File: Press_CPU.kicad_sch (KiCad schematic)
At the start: 100 parts, among them J2 2-215079-0, J3 Conn_01x16, J4 Conn_01x16, U1 APM32F405RGT6, U10 LMV321, U11 LMV321, U12 FM25W256, U13 LMV321, U14 LMV321, U15 LMV321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

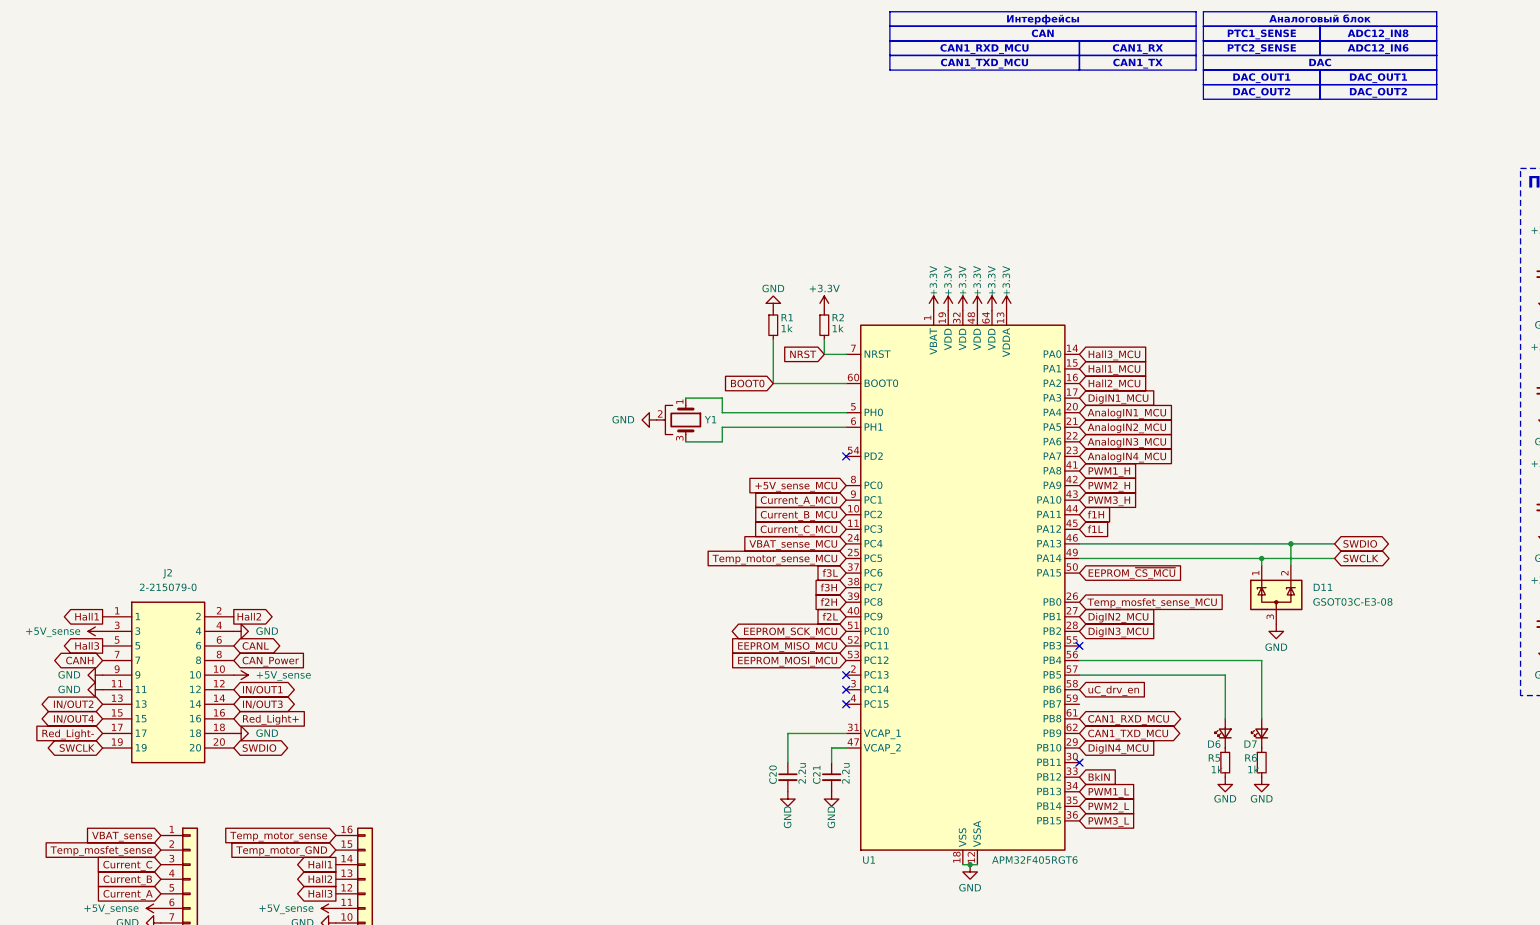
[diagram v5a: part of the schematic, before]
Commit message: VER1.0: первая готовая трассировка, требует обсуждения
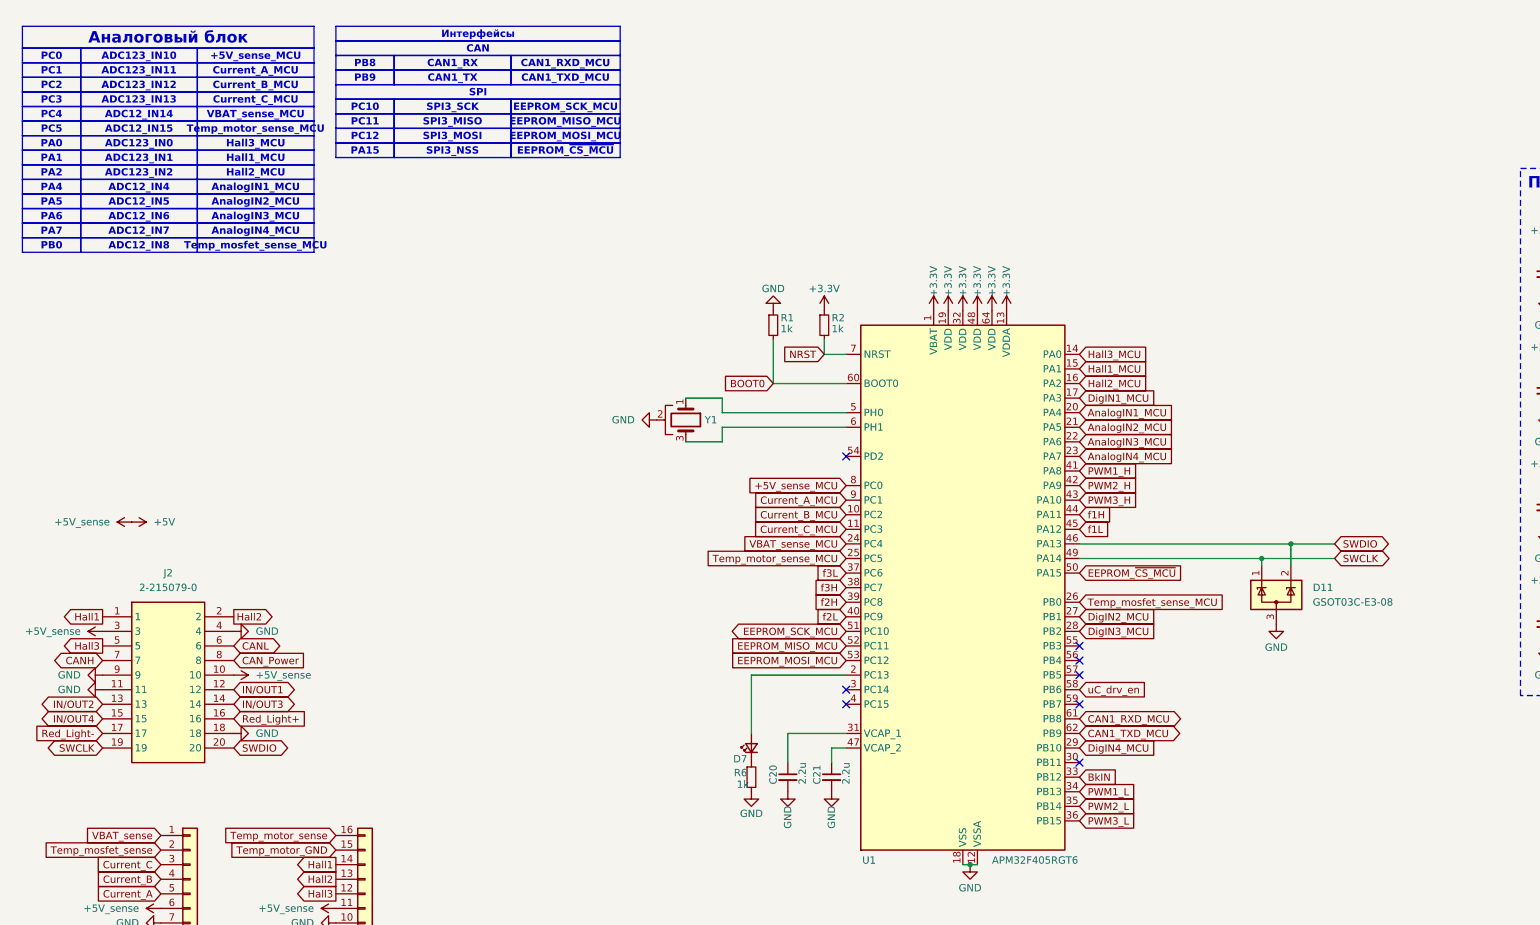
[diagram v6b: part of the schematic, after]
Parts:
- removed D6: ~, LED_SMD:LED_0603_1608Metric_Pad1.05x0.95mm_HandSolder, symbol Device:LED_Small
- removed R5: 1k, Resistor_SMD:R_0603_1608Metric_Pad0.98x0.95mm_HandSolder, symbol Device:R_Small
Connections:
- net +5V_sense is gone; now on net +5V: J2.10, J2.3, J3.6 (Pin_6), J4.11 (Pin_11), R65.1, R66.1
- net at U1.2 (PC13): now also D7.2 (A)
- net at U1.56 (PB4): no longer D7.2 (A)
- no-connect marks 11 -> 13
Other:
- moved on the sheet: D7, R6

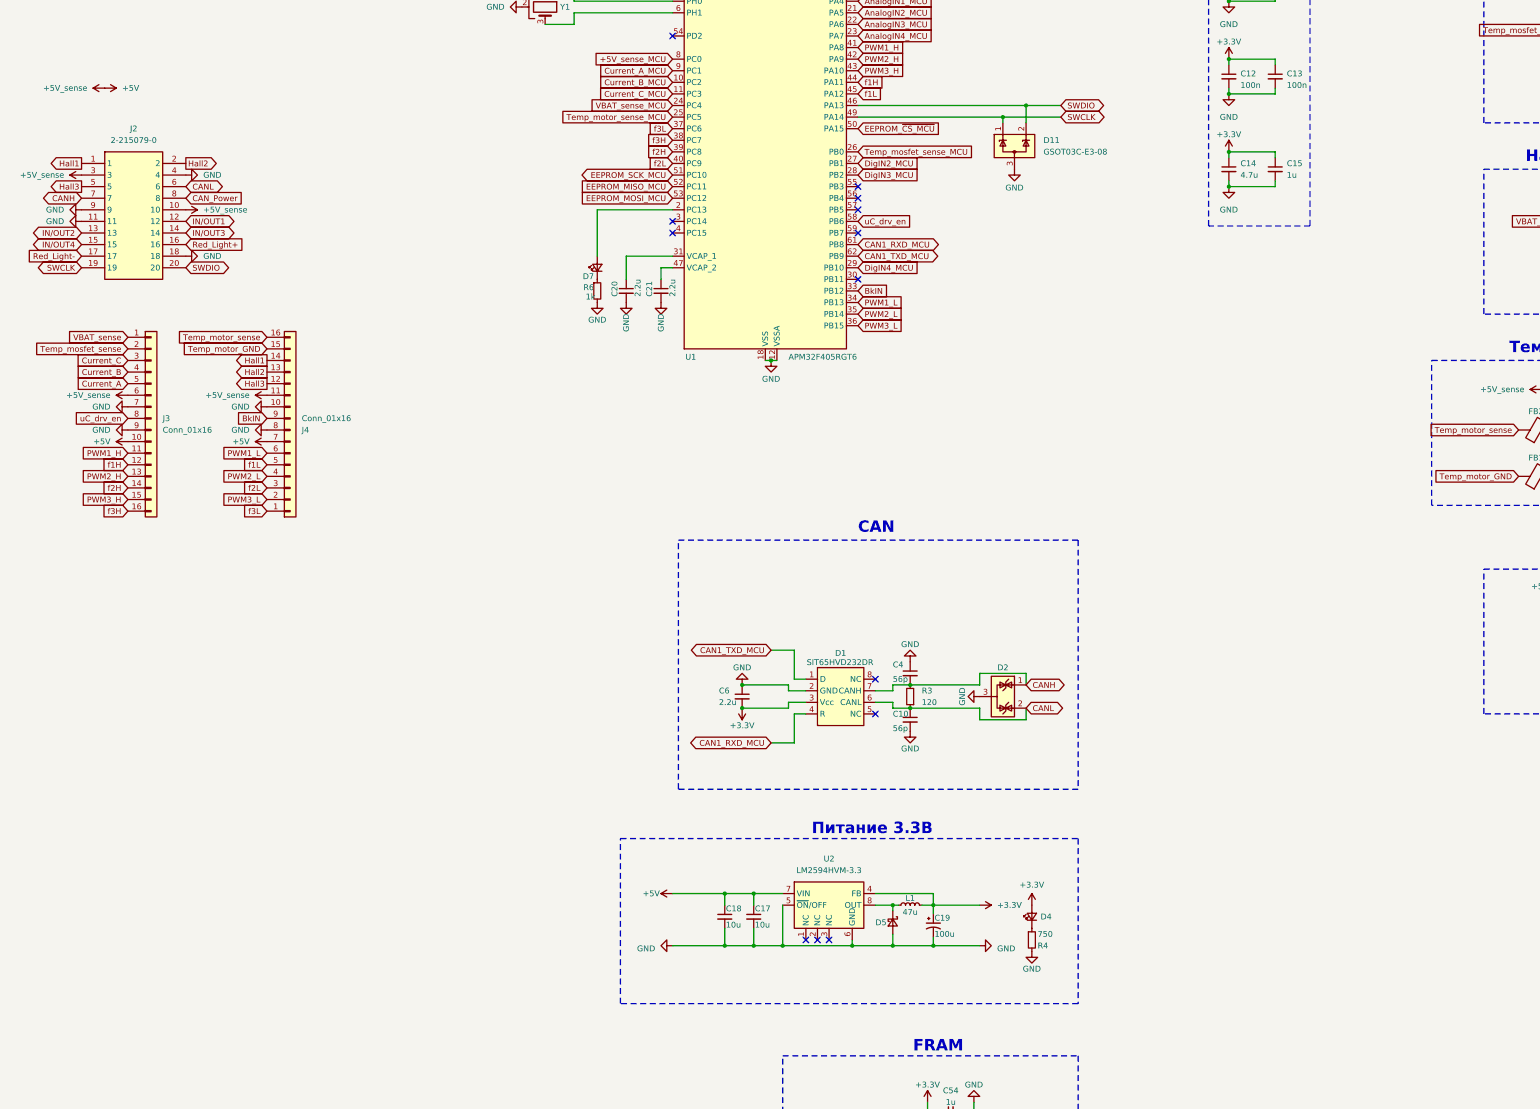
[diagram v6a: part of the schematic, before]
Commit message: VER1.0: добавил предохранители по питанию датчиков и внешнего CAN
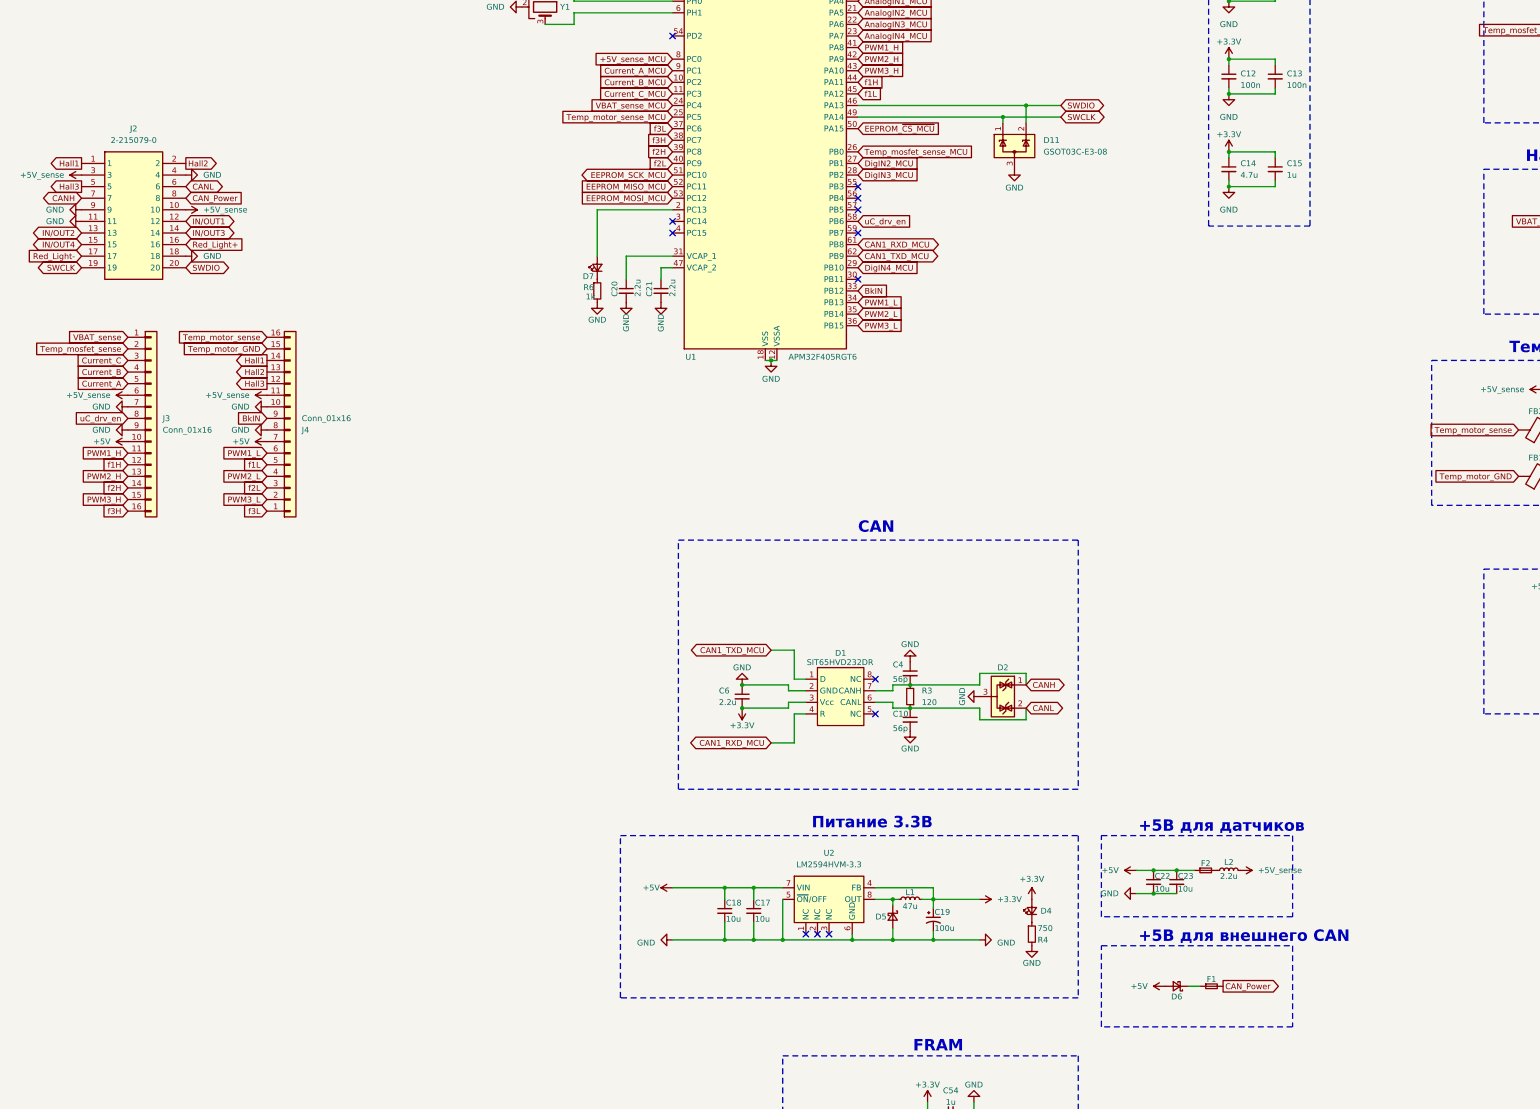
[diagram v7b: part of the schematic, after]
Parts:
- added C22, C23: 10u, Capacitor_SMD:C_0805_2012Metric_Pad1.18x1.45mm_HandSolder, symbol Device:C_Small
- added D6: D_Schottky_Small, Diode_SMD:D_SOD-323_HandSoldering, symbol Device:D_Schottky_Small
- added F1, F2: Fuse_Small, Fuse:Fuse_0805_2012Metric_Pad1.15x1.40mm_HandSolder, symbol Device:Fuse_Small
- added L2: 2.2u, Inductor_SMD:L_1210_3225Metric_Pad1.42x2.65mm_HandSolder, symbol Device:L_Small
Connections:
- net +5V: now also C22.1, C23.1, D6.2 (A), F2.1; no longer J2.10, J2.3, J3.6 (Pin_6), J4.11 (Pin_11), R65.1, R66.1
- net CAN_Power: now also F1.2
- net GND: now also C22.2, C23.2
- new net: F2.2, L2.1
- new net: D6.1 (K), F1.1
- new net +5V_sense: J2.10, J2.3, J3.6 (Pin_6), J4.11 (Pin_11), L2.2, R65.1, R66.1
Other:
- note added: "+5В для внешнего CAN"
- note added: "+5В для датчиков"
- moved on the sheet: C17, C18, C19, D4, D5, L1, R4, U2

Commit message: VER1.0: добавил шелкографию с версией
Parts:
- D10, D11, D3, D8, D9: value GSOT03C-E3-08 -> ~; Product Name (none) -> GSOT03C-E3-08
- D4: Product Name FYLS-0805UYC -> FYLS-0603UYC
- D5: value MBRA320 -> ~; Product Name (none) -> MBRA320
- D6: value D_Schottky_Small -> ~; Product Name (none) -> BAT46JFILM
- D7: Product Name FYLS-0805UBC -> FYLS-0603UBC
- F1, F2: value Fuse_Small -> ~; Description P/N (none) -> Fuse; Product Name (none) -> MF-PSMF050X-2
- FB1, FB2: value BLM21AG102SN1D -> ~; Product Name (none) -> BLM21AG102SN1D
- J2: value 2-215079-0 -> ~; Product Name (none) -> 2-215079-0
- J3, J4: value Conn_01x16 -> ~; Product Name (none) -> DS-1025-05 - 2x20
- L1: Product Name (none) -> NLC453232T-470K-PF
- L2: Product Name (none) -> CM322522-2R2KL
- U1: value APM32F405RGT6 -> ~; Product Name (none) -> APM32F405RGT6
- U10, U11, U13, U14, U15, U16: value LMV321 -> ~; Product Name (none) -> LMV321
- U12: value FM25W256 -> ~; Product Name (none) -> FM25W256
- U2: value LM2594HVM-3.3 -> ~; Product Name (none) -> LM2594HVM-3.3
- Y1: value CSTCE8M00G55A-R0 -> ~; Product Name (none) -> CSTCE8M00G55A-R0
